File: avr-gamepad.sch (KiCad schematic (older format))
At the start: 32 parts, among them J1 Conn_01x08, J2 Conn_01x08, P1 USB_C_Plug_USB2.0, SW1 RESET, SW10 Up, SW11 Down, SW12 Left, SW13 Select, SW2 R, SW3 X, SW4 A, SW5 B, SW6 Start, SW7 Y, SW8 Right, SW9 L, U1 ATmega32U4-AU, Y1 16 MHz

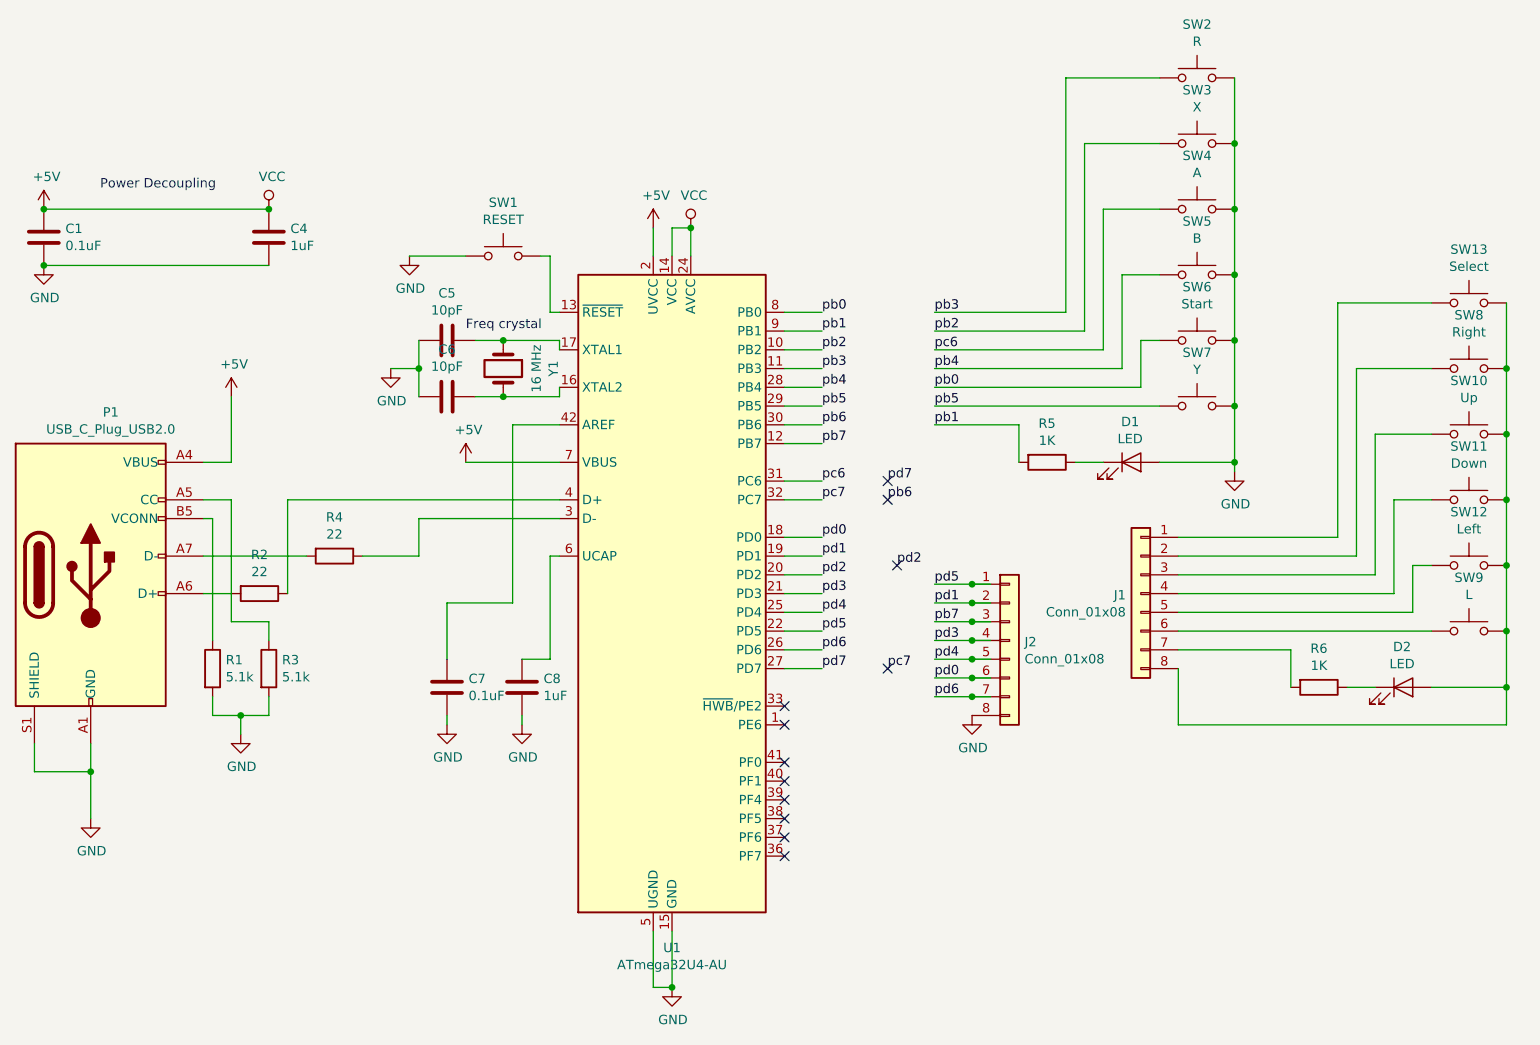
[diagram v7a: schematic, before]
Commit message: component relabelling, shuffling around, two-piece board
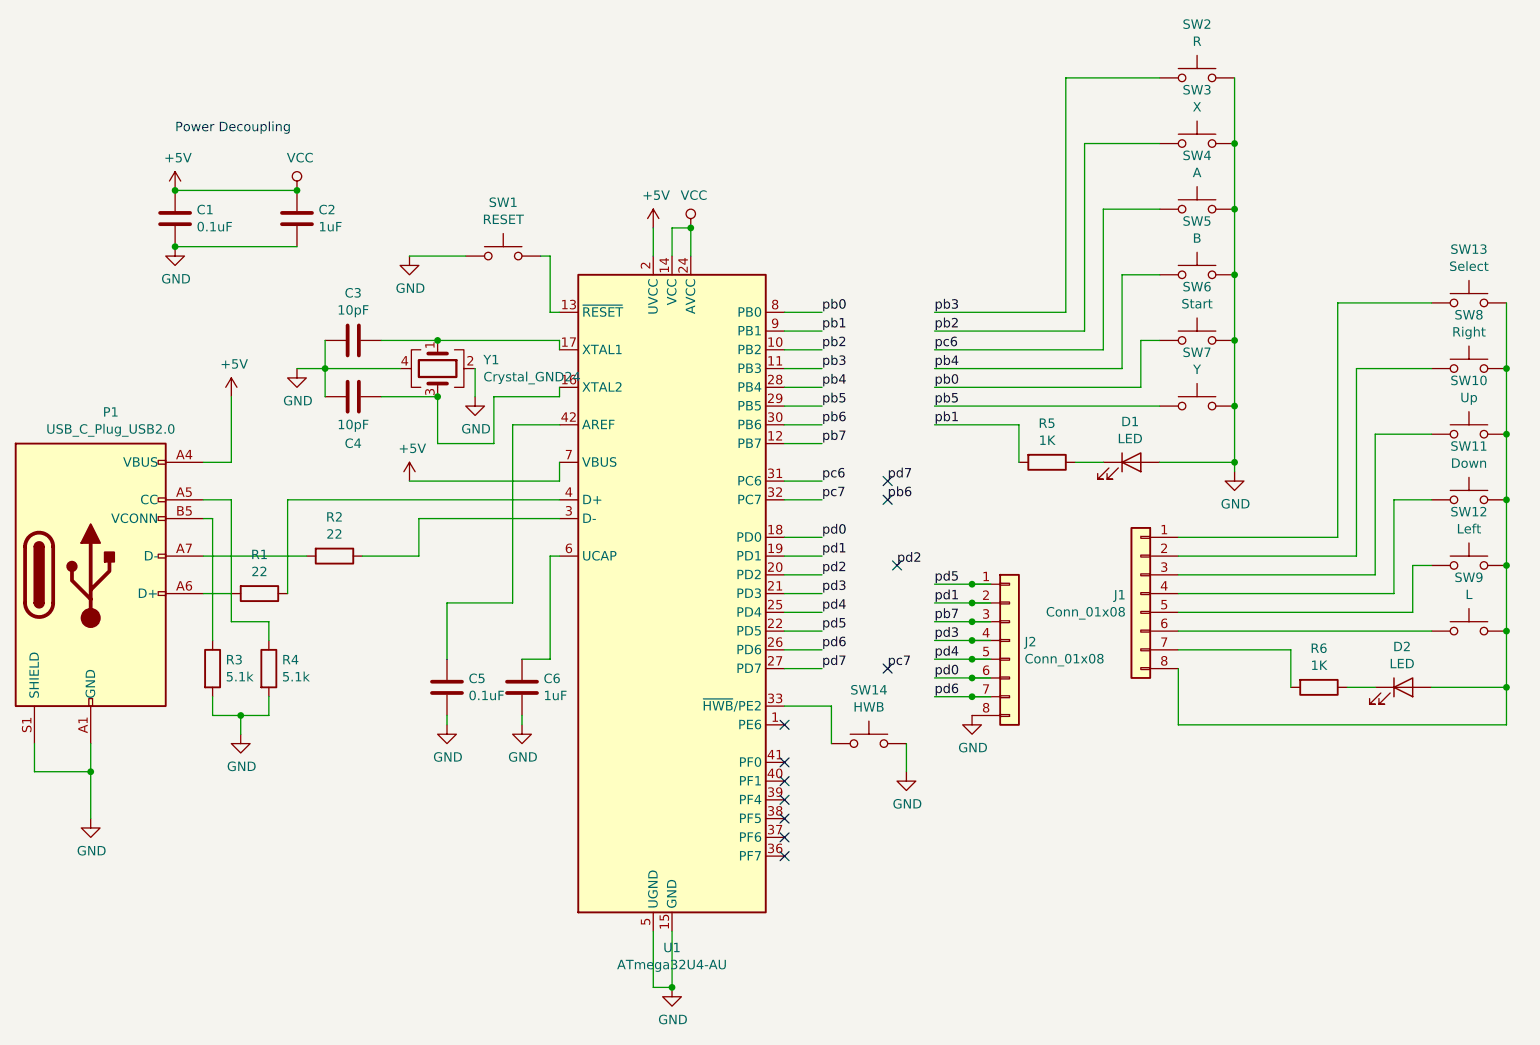
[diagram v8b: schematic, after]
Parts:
- removed Y1: 16 MHz, Crystal:Crystal_SMD_SeikoEpson_FA238-4Pin_3.2x2.5mm, symbol Device:Crystal
- added SW14: HWB, button-contacts:Small, symbol Switch:SW_Push
- added Y1: Crystal_GND24, Crystal:Crystal_SMD_SeikoEpson_FA238-4Pin_3.2x2.5mm, symbol Device:Crystal_GND24
- renumbered C4 to C2, C5 to C3, C6 to C4, C7 to C5, C8 to C6, R2 to R1, R4 to R2, R1 to R3, R3 to R4
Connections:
- wire segments 144 -> 153
- no-connect marks 12 -> 11
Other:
- note removed: "Freq crystal"
- moved on the sheet: C1, C2, C3, C4
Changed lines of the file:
@@
 $EndDescr
 $Comp
-L Device:R R2
+L Device:R R1
 U 1 1 5CDE5E2E
 P 2300 3600
-F 0 "R2" V 2093 3600 50  0000 C CNN
+F 0 "R1" V 2093 3600 50  0000 C CNN
 F 1 "22" V 2184 3600 50  0000 C CNN
 F 2 "Resistor_SMD:R_0805_2012Metric" V 2230 3600 50  0001 C CNN
@@
 L power:+5V #PWR0101
 U 1 1 5CDF4CB6
-P 3400 2900
-F 0 "#PWR0101" H 3400 2750 50  0001 C CNN
-F 1 "+5V" H 3415 3073 50  0000 C CNN
-F 2 "" H 3400 2900 50  0001 C CNN
-F 3 "" H 3400 2900 50  0001 C CNN
-	1    3400 2900
+P 3100 3000
+F 0 "#PWR0101" H 3100 2850 50  0001 C CNN
+F 1 "+5V" H 3115 3173 50  0000 C CNN
+F 2 "" H 3100 3000 50  0001 C CNN
+F 3 "" H 3100 3000 50  0001 C CNN
+	1    3100 3000
 	1    0    0    -1
 $EndComp
@@
 	4400 1650 4400 1800
 $Comp
-L Device:Crystal Y1
-U 1 1 5CE113E3
-P 3600 2400
-F 0 "Y1" H 3600 2668 50  0000 C CNN
-F 1 "16 MHz" H 3600 2577 50  0000 C CNN
-F 2 "Crystal:Crystal_SMD_SeikoEpson_FA238-4Pin_3.2x2.5mm" H 3600 2400 50  0001 C CNN
-F 3 "~" H 3600 2400 50  0001 C CNN
-	1    3600 2400
-	0    1    1    0
-$EndComp
-$Comp
-L Device:R R4
+L Device:R R2
 U 1 1 5CDE68D4
 P 2700 3400
-F 0 "R4" V 2493 3400 50  0000 C CNN
+F 0 "R2" V 2493 3400 50  0000 C CNN
 F 1 "22" V 2584 3400 50  0000 C CNN
 F 2 "Resistor_SMD:R_0805_2012Metric" V 2630 3400 50  0001 C CNN
@@
 	3900 2500 3900 2550
 Wire Wire Line
-	3900 2550 3600 2550
-Wire Wire Line
 	3900 2300 3900 2250
-Wire Wire Line
-	3900 2250 3600 2250
 $Comp
 L power:GND #PWR0105
 U 1 1 5CE2A20B
-P 3000 2400
-F 0 "#PWR0105" H 3000 2150 50  0001 C CNN
-F 1 "GND" H 3005 2227 50  0000 C CNN
-F 2 "" H 3000 2400 50  0001 C CNN
-F 3 "" H 3000 2400 50  0001 C CNN
-	1    3000 2400
-	1    0    0    -1
-$EndComp
-Wire Wire Line
-	3150 2250 3150 2400
-Wire Wire Line
-	3150 2400 3000 2400
-Wire Wire Line
-	3150 2550 3150 2400
-Connection ~ 3150 2400
-Text Notes 3400 2200 0    50   ~ 0
-Freq crystal
+P 2500 2400
+F 0 "#PWR0105" H 2500 2150 50  0001 C CNN
+F 1 "GND" H 2505 2227 50  0000 C CNN
+F 2 "" H 2500 2400 50  0001 C CNN
+F 3 "" H 2500 2400 50  0001 C CNN
+	1    2500 2400
+	1    0    0    -1
+$EndComp
+Wire Wire Line
+	2650 2250 2650 2400
+Wire Wire Line
+	2650 2400 2500 2400
+Wire Wire Line
+	2650 2550 2650 2400
+Connection ~ 2650 2400
 Wire Wire Line
 	2000 2900 2150 2900
@@
 L power:VCC #PWR0107
 U 1 1 5CE2CBD3
-P 2350 1550
-F 0 "#PWR0107" H 2350 1400 50  0001 C CNN
-F 1 "VCC" H 2367 1723 50  0000 C CNN
-F 2 "" H 2350 1550 50  0001 C CNN
-F 3 "" H 2350 1550 50  0001 C CNN
-	1    2350 1550
-	1    0    0    -1
-$EndComp
-Text Notes 1450 1450 0    50   ~ 0
+P 2500 1450
+F 0 "#PWR0107" H 2500 1300 50  0001 C CNN
+F 1 "VCC" H 2517 1623 50  0000 C CNN
+F 2 "" H 2500 1450 50  0001 C CNN
+F 3 "" H 2500 1450 50  0001 C CNN
+	1    2500 1450
+	1    0    0    -1
+$EndComp
+Text Notes 1850 1150 0    50   ~ 0
 Power Decoupling
 $Comp
 L power:+5V #PWR0108
 U 1 1 5CE0A7FF
-P 1150 1550
-F 0 "#PWR0108" H 1150 1400 50  0001 C CNN
-F 1 "+5V" H 1165 1723 50  0000 C CNN
-F 2 "" H 1150 1550 50  0001 C CNN
-F 3 "" H 1150 1550 50  0001 C CNN
-	1    1150 1550
+P 1850 1450
+F 0 "#PWR0108" H 1850 1300 50  0001 C CNN
+F 1 "+5V" H 1865 1623 50  0000 C CNN
+F 2 "" H 1850 1450 50  0001 C CNN
+F 3 "" H 1850 1450 50  0001 C CNN
+	1    1850 1450
 	1    0    0    -1
 $EndComp
@@
 L power:GND #PWR0109
 U 1 1 5CE0A1B4
-P 1150 1850
-F 0 "#PWR0109" H 1150 1600 50  0001 C CNN
-F 1 "GND" H 1155 1677 50  0000 C CNN
-F 2 "" H 1150 1850 50  0001 C CNN
-F 3 "" H 1150 1850 50  0001 C CNN
-	1    1150 1850
+P 1850 1750
+F 0 "#PWR0109" H 1850 1500 50  0001 C CNN
+F 1 "GND" H 1855 1577 50  0000 C CNN
+F 2 "" H 1850 1750 50  0001 C CNN
+F 3 "" H 1850 1750 50  0001 C CNN
+	1    1850 1750
 	1    0    0    -1
 $EndComp
@@
 L Device:C C1
 U 1 1 5CE336BE
-P 1150 1700
-F 0 "C1" H 1265 1746 50  0000 L CNN
-F 1 "0.1uF" H 1265 1655 50  0000 L CNN
-F 2 "Capacitor_SMD:C_0805_2012Metric" H 1150 1700 50  0001 C CNN
-F 3 "~" H 1150 1700 50  0001 C CNN
-	1    1150 1700
-	1    0    0    -1
-$EndComp
-Connection ~ 1150 1550
-Connection ~ 1150 1850
+P 1850 1600
+F 0 "C1" H 1965 1646 50  0000 L CNN
+F 1 "0.1uF" H 1965 1555 50  0000 L CNN
+F 2 "Capacitor_SMD:C_0805_2012Metric" H 1850 1600 50  0001 C CNN
+F 3 "~" H 1850 1600 50  0001 C CNN
+	1    1850 1600
+	1    0    0    -1
+$EndComp
+Connection ~ 1850 1450
+Connection ~ 1850 1750
+$Comp
+L Device:C C2
+U 1 1 5CE34260
+P 2500 1600
+F 0 "C2" H 2615 1646 50  0000 L CNN
+F 1 "1uF" H 2615 1555 50  0000 L CNN
+F 2 "Capacitor_SMD:C_0805_2012Metric" H 2500 1600 50  0001 C CNN
+F 3 "~" H 2500 1600 50  0001 C CNN
+	1    2500 1600
+	1    0    0    -1
+$EndComp
+$Comp
+L Device:C C3
+U 1 1 5CE36ECF
+P 2800 2250
+F 0 "C3" V 2548 2250 50  0000 C CNN
+F 1 "10pF" V 2639 2250 50  0000 C CNN
+F 2 "Capacitor_SMD:C_0805_2012Metric" H 2800 2250 50  0001 C CNN
+F 3 "~" H 2800 2250 50  0001 C CNN
+	1    2800 2250
+	0    1    1    0
+$EndComp
 $Comp
 L Device:C C4
-U 1 1 5CE34260
-P 2350 1700
-F 0 "C4" H 2465 1746 50  0000 L CNN
-F 1 "1uF" H 2465 1655 50  0000 L CNN
-F 2 "Capacitor_SMD:C_0805_2012Metric" H 2350 1700 50  0001 C CNN
-F 3 "~" H 2350 1700 50  0001 C CNN
-	1    2350 1700
-	1    0    0    -1
-$EndComp
-Connection ~ 2350 1550
-$Comp
-L Device:C C5
-U 1 1 5CE36ECF
-P 3300 2250
-F 0 "C5" V 3048 2250 50  0000 C CNN
-F 1 "10pF" V 3139 2250 50  0000 C CNN
-F 2 "Capacitor_SMD:C_0805_2012Metric" H 3300 2250 50  0001 C CNN
-F 3 "~" H 3300 2250 50  0001 C CNN
-	1    3300 2250
-	0    1    1    0
-$EndComp
-$Comp
-L Device:C C6
 U 1 1 5CE373C9
-P 3300 2550
-F 0 "C6" V 3048 2550 50  0000 C CNN
-F 1 "10pF" V 3139 2550 50  0000 C CNN
-F 2 "Capacitor_SMD:C_0805_2012Metric" H 3300 2550 50  0001 C CNN
-F 3 "~" H 3300 2550 50  0001 C CNN
-	1    3300 2550
+P 2800 2550
+F 0 "C4" V 3050 2550 50  0000 C CNN
+F 1 "10pF" V 2950 2550 50  0000 C CNN
+F 2 "Capacitor_SMD:C_0805_2012Metric" H 2800 2550 50  0001 C CNN
+F 3 "~" H 2800 2550 50  0001 C CNN
+	1    2800 2550
 	0    1    1    0
 $EndComp
@@
 	3850 3400 3900 3400
 $Comp
-L Device:C C8
+L Device:C C6
 U 1 1 5CE37ACD
 P 3700 4100
-F 0 "C8" H 3815 4146 50  0000 L CNN
+F 0 "C6" H 3815 4146 50  0000 L CNN
 F 1 "1uF" H 3815 4055 50  0000 L CNN
 F 2 "Capacitor_SMD:C_0805_2012Metric" H 3700 4100 50  0001 C CNN
@@
 	3650 3650 3300 3650
 $Comp
-L Device:C C7
+L Device:C C5
 U 1 1 5CE3DF92
 P 3300 4100
-F 0 "C7" H 3415 4146 50  0000 L CNN
+F 0 "C5" H 3415 4146 50  0000 L CNN
 F 1 "0.1uF" H 3415 4055 50  0000 L CNN
 F 2 "Capacitor_SMD:C_0805_2012Metric" H 3300 4100 50  0001 C CNN
@@
 Connection ~ 7500 2600
 Connection ~ 7500 2900
-Wire Wire Line
-	3450 2550 3600 2550
-Connection ~ 3600 2550
-Wire Wire Line
-	3450 2250 3600 2250
-Connection ~ 3600 2250
-NoConn ~ 5100 4200
 NoConn ~ 5100 4500
 NoConn ~ 5100 4600
@@
 	2000 3100 2150 3100
 $Comp
-L Device:R R3
+L Device:R R4
 U 1 1 5CE8517A
 P 2350 4000
-F 0 "R3" H 2420 4046 50  0000 L CNN
+F 0 "R4" H 2420 4046 50  0000 L CNN
 F 1 "5.1k" H 2420 3955 50  0000 L CNN
 F 2 "Resistor_SMD:R_0805_2012Metric" V 2280 4000 50  0001 C CNN
@@
 	2150 3100 2150 3750
 $Comp
-L Device:R R1
+L Device:R R3
 U 1 1 5CE91027
 P 2050 4000
-F 0 "R1" H 2120 4046 50  0000 L CNN
+F 0 "R3" H 2120 4046 50  0000 L CNN
 F 1 "5.1k" H 2120 3955 50  0000 L CNN
 F 2 "Resistor_SMD:R_0805_2012Metric" V 1980 4000 50  0001 C CNN
@@
 Wire Wire Line
 	3300 4250 3300 4300
-Wire Wire Line
-	3400 2900 3900 2900
 Wire Wire Line
 	2050 4250 2200 4250
@@
 Wire Wire Line
 	3100 1800 3400 1800
-Wire Wire Line
-	1150 1550 2350 1550
-Wire Wire Line
-	1150 1850 2350 1850
 $Comp
 L Connector_Generic:Conn_01x08 J2
@@
 Wire Wire Line
 	8950 4100 8950 4300
+$Comp
+L Device:Crystal_GND24 Y1
+U 1 1 5D9AE8A9
+P 3250 2400
+F 0 "Y1" V 3204 2644 50  0000 L CNN
+F 1 "Crystal_GND24" V 3295 2644 50  0000 L CNN
+F 2 "Crystal:Crystal_SMD_SeikoEpson_FA238-4Pin_3.2x2.5mm" H 3250 2400 50  0001 C CNN
+F 3 "~" H 3250 2400 50  0001 C CNN
+	1    3250 2400
+	0    1    1    0
+$EndComp
+Wire Wire Line
+	2950 2250 3250 2250
+Wire Wire Line
+	3050 2400 2650 2400
+$Comp
+L power:GND #PWR0114
+U 1 1 5D9DC9EB
+P 3450 2550
+F 0 "#PWR0114" H 3450 2300 50  0001 C CNN
+F 1 "GND" H 3455 2377 50  0000 C CNN
+F 2 "" H 3450 2550 50  0001 C CNN
+F 3 "" H 3450 2550 50  0001 C CNN
+	1    3450 2550
+	1    0    0    -1
+$EndComp
+Wire Wire Line
+	3450 2550 3450 2400
+Wire Wire Line
+	3900 2550 3550 2550
+Wire Wire Line
+	3550 2550 3550 2800
+Wire Wire Line
+	3550 2800 3250 2800
+Wire Wire Line
+	3250 2800 3250 2550
+Wire Wire Line
+	2950 2550 3250 2550
+Connection ~ 3250 2550
+Wire Wire Line
+	3250 2250 3900 2250
+Connection ~ 3250 2250
+Wire Wire Line
+	3900 2900 3900 3000
+Wire Wire Line
+	3900 3000 3100 3000
+Wire Wire Line
+	1850 1750 2500 1750
+Connection ~ 2500 1450
+Wire Wire Line
+	1850 1450 2500 1450
+$Comp
+L Switch:SW_Push SW14
+U 1 1 5DA27F25
+P 5550 4400
+F 0 "SW14" H 5550 4685 50  0000 C CNN
+F 1 "HWB" H 5550 4594 50  0000 C CNN
+F 2 "button-contacts:Small" H 5550 4600 50  0001 C CNN
+F 3 "~" H 5550 4600 50  0001 C CNN
+	1    5550 4400
+	1    0    0    -1
+$EndComp
+Wire Wire Line
+	5100 4200 5350 4200
+Wire Wire Line
+	5350 4200 5350 4400
+$Comp
+L power:GND #PWR03
+U 1 1 5DA2FA34
+P 5750 4550
+F 0 "#PWR03" H 5750 4300 50  0001 C CNN
+F 1 "GND" H 5755 4377 50  0000 C CNN
+F 2 "" H 5750 4550 50  0001 C CNN
+F 3 "" H 5750 4550 50  0001 C CNN
+	1    5750 4550
+	1    0    0    -1
+$EndComp
+Wire Wire Line
+	5750 4550 5750 4400
 $EndSCHEMATC
